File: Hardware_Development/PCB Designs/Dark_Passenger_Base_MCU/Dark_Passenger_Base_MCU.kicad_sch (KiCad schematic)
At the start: 26 parts, among them J1 Conn_01x22, J10 SPARE I2C, J11 IMU, J12 Toggle Switches, J13 Spare, J14 Motor Encoder 1, J15 Motor Encoder 2, J16 RESET, J18 Motor Control, J2 Conn_01x22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

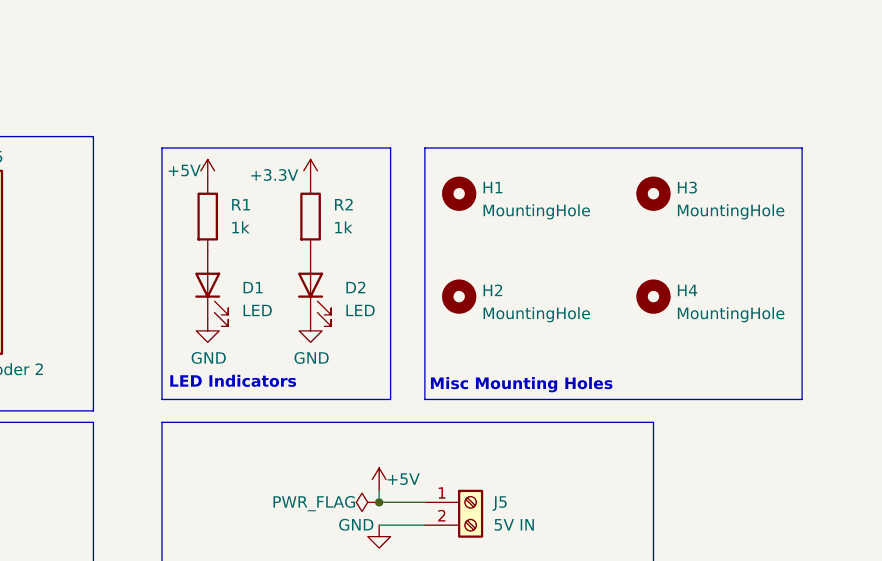
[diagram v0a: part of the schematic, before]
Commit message: Updates to code based on new pinouts from PCBs
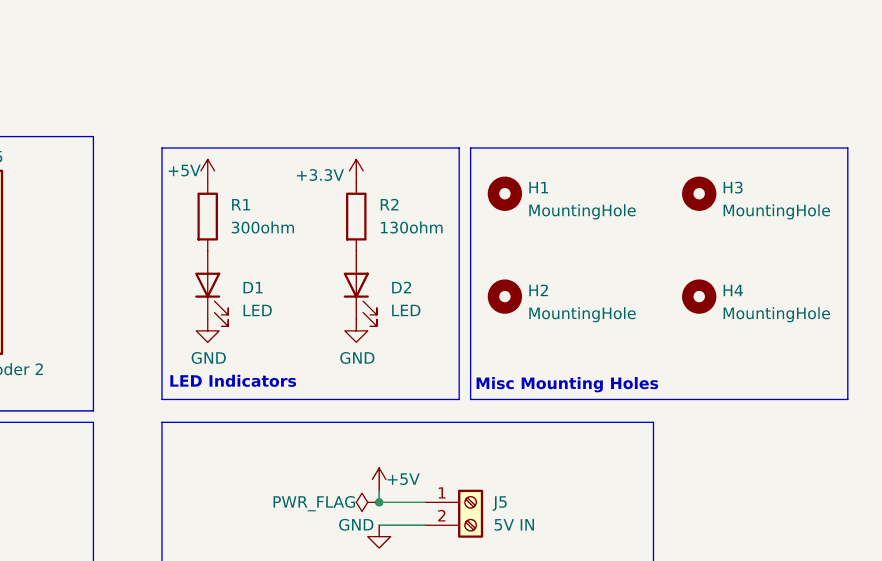
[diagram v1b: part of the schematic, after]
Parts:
- R1: value 1k -> 300ohm
- R2: value 1k -> 130ohm
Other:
- moved on the sheet: D2, H1, H2, H3, H4, R2
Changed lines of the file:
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@@
 	(rectangle
 		(start 175.26 26.67)
-		(end 200.66 54.61)
+		(end 208.28 54.61)
 		(stroke
 			(width 0)
@@
 	)
 	(rectangle
-		(start 204.47 26.67)
-		(end 246.38 54.61)
+		(start 209.55 26.67)
+		(end 251.46 54.61)
 		(stroke
 			(width 0)
@@
 	(text "Misc Mounting Holes"
 		(exclude_from_sim no)
-		(at 204.978 53.848 0)
+		(at 210.058 53.848 0)
 		(effects
 			(font
@@
 		(on_board yes)
 		(dnp no)
-		(fields_autoplaced yes)
 		(property "Reference" "R1"
 			(at 182.88 33.0199 0)
@@
 			)
 		)
-		(property "Value" "1k"
+		(property "Value" "300ohm"
 			(at 182.88 35.5599 0)
 			(effects
@@
 	(symbol
 		(lib_id "Device:R")
-		(at 191.77 34.29 0)
+		(at 196.85 34.29 0)
 		(unit 1)
 		(exclude_from_sim no)
@@
 		(fields_autoplaced yes)
 		(property "Reference" "R2"
-			(at 194.31 33.0199 0)
+			(at 199.39 33.0199 0)
 			(effects
 				(font
@@
 			)
 		)
-		(property "Value" "1k"
-			(at 194.31 35.5599 0)
+		(property "Value" "130ohm"
+			(at 199.39 35.5599 0)
 			(effects
 				(font
@@
 		)
 		(property "Footprint" "Resistor_SMD:R_1206_3216Metric_Pad1.30x1.75mm_HandSolder"
-			(at 189.992 34.29 90)
+			(at 195.072 34.29 90)
 			(effects
 				(font
@@
 		)
 		(property "Datasheet" "~"
-			(at 191.77 34.29 0)
+			(at 196.85 34.29 0)
 			(effects
 				(font
@@
 		)
 		(property "Description" ""
-			(at 191.77 34.29 0)
+			(at 196.85 34.29 0)
 			(effects
 				(font
@@
 	(symbol
 		(lib_id "power:GND")
-		(at 191.77 45.72 0)
+		(at 196.85 45.72 0)
 		(unit 1)
 		(exclude_from_sim no)
@@
 		(dnp no)
 		(property "Reference" "#PWR028"
-			(at 191.77 52.07 0)
+			(at 196.85 52.07 0)
 			(effects
 				(font
@@
 		)
 		(property "Value" "GND"
-			(at 191.8843 50.0444 0)
+			(at 196.9643 50.0444 0)
 			(effects
 				(font
@@
 		)
 		(property "Footprint" ""
-			(at 191.77 45.72 0)
+			(at 196.85 45.72 0)
 			(effects
 				(font
@@
 		)
 		(property "Datasheet" ""
-			(at 191.77 45.72 0)
+			(at 196.85 45.72 0)
 			(effects
 				(font
@@
 		)
 		(property "Description" ""
-			(at 191.77 45.72 0)
+			(at 196.85 45.72 0)
 			(effects
 				(font
@@
 	(symbol
 		(lib_id "Mechanical:MountingHole")
-		(at 208.28 43.18 0)
+		(at 213.36 43.18 0)
 		(unit 1)
 		(exclude_from_sim no)
@@
 		(dnp no)
 		(property "Reference" "H2"
-			(at 210.82 42.545 0)
+			(at 215.9 42.545 0)
 			(effects
 				(font
@@
 		)
 		(property "Value" "MountingHole"
-			(at 210.82 45.085 0)
+			(at 215.9 45.085 0)
 			(effects
 				(font
@@
 		)
 		(property "Footprint" "MountingHole:MountingHole_3mm"
-			(at 208.28 43.18 0)
+			(at 213.36 43.18 0)
 			(effects
 				(font
@@
 		)
 		(property "Datasheet" "~"
-			(at 208.28 43.18 0)
+			(at 213.36 43.18 0)
 			(effects
 				(font
@@
 		)
 		(property "Description" ""
-			(at 208.28 43.18 0)
+			(at 213.36 43.18 0)
 			(effects
 				(font
@@
 	(symbol
 		(lib_id "Mechanical:MountingHole")
-		(at 208.28 31.75 0)
+		(at 213.36 31.75 0)
 		(unit 1)
 		(exclude_from_sim no)
@@
 		(dnp no)
 		(property "Reference" "H1"
-			(at 210.82 31.115 0)
+			(at 215.9 31.115 0)
 			(effects
 				(font
@@
 		)
 		(property "Value" "MountingHole"
-			(at 210.82 33.655 0)
+			(at 215.9 33.655 0)
 			(effects
 				(font
@@
 		)
 		(property "Footprint" "MountingHole:MountingHole_3mm"
-			(at 208.28 31.75 0)
+			(at 213.36 31.75 0)
 			(effects
 				(font
@@
 		)
 		(property "Datasheet" "~"
-			(at 208.28 31.75 0)
+			(at 213.36 31.75 0)
 			(effects
 				(font
@@
 		)
 		(property "Description" ""
-			(at 208.28 31.75 0)
+			(at 213.36 31.75 0)
 			(effects
 				(font
@@
 		(lib_name "LED_1")
 		(lib_id "Device:LED")
-		(at 191.77 41.91 90)
+		(at 196.85 41.91 90)
 		(unit 1)
 		(exclude_from_sim no)
@@
 		(fields_autoplaced yes)
 		(property "Reference" "D2"
-			(at 195.58 42.2274 90)
+			(at 200.66 42.2274 90)
 			(effects
 				(font
@@
 		)
 		(property "Value" "LED"
-			(at 195.58 44.7674 90)
+			(at 200.66 44.7674 90)
 			(effects
 				(font
@@
 		)
 		(property "Footprint" "LED_SMD:LED_1206_3216Metric_Pad1.42x1.75mm_HandSolder"
-			(at 191.77 41.91 0)
+			(at 196.85 41.91 0)
 			(effects
 				(font
@@
 		)
 		(property "Datasheet" "~"
-			(at 191.77 41.91 0)
+			(at 196.85 41.91 0)
 			(effects
 				(font
@@
 		)
 		(property "Description" "Light emitting diode"
-			(at 191.77 41.91 0)
+			(at 196.85 41.91 0)
 			(effects
 				(font
@@
 		)
 		(property "Sim.Pins" "1=K 2=A"
-			(at 191.77 41.91 0)
+			(at 196.85 41.91 0)
 			(effects
 				(font
@@
 	(symbol
 		(lib_id "power:+3.3V")
-		(at 191.77 30.48 0)
+		(at 196.85 30.48 0)
 		(unit 1)
 		(exclude_from_sim no)
@@
 		(dnp no)
 		(property "Reference" "#PWR041"
-			(at 191.77 34.29 0)
+			(at 196.85 34.29 0)
 			(effects
 				(font
@@
 		)
 		(property "Value" "+3.3V"
-			(at 187.706 29.718 0)
+			(at 192.786 29.718 0)
 			(effects
 				(font
@@
 		)
 		(property "Footprint" ""
-			(at 191.77 30.48 0)
+			(at 196.85 30.48 0)
 			(effects
 				(font
@@
 		)
 		(property "Datasheet" ""
-			(at 191.77 30.48 0)
+			(at 196.85 30.48 0)
 			(effects
 				(font
@@
 		)
 		(property "Description" "Power symbol creates a global label with name \"+3.3V\""
-			(at 191.77 30.48 0)
+			(at 196.85 30.48 0)
 			(effects
 				(font
@@
 	(symbol
 		(lib_id "Mechanical:MountingHole")
-		(at 229.87 43.18 0)
+		(at 234.95 43.18 0)
 		(unit 1)
 		(exclude_from_sim no)
@@
 		(dnp no)
 		(property "Reference" "H4"
-			(at 232.41 42.545 0)
+			(at 237.49 42.545 0)
 			(effects
 				(font
@@
 		)
 		(property "Value" "MountingHole"
-			(at 232.41 45.085 0)
+			(at 237.49 45.085 0)
 			(effects
 				(font
@@
 		)
 		(property "Footprint" "MountingHole:MountingHole_3mm"
-			(at 229.87 43.18 0)
+			(at 234.95 43.18 0)
 			(effects
 				(font
@@
 		)
 		(property "Datasheet" "~"
-			(at 229.87 43.18 0)
+			(at 234.95 43.18 0)
 			(effects
 				(font
@@
 		)
 		(property "Description" ""
-			(at 229.87 43.18 0)
+			(at 234.95 43.18 0)
 			(effects
 				(font
@@
 	(symbol
 		(lib_id "Mechanical:MountingHole")
-		(at 229.87 31.75 0)
+		(at 234.95 31.75 0)
 		(unit 1)
 		(exclude_from_sim no)
@@
 		(fields_autoplaced yes)
 		(property "Reference" "H3"
-			(at 232.41 31.115 0)
+			(at 237.49 31.115 0)
 			(effects
 				(font
@@
 		)
 		(property "Value" "MountingHole"
-			(at 232.41 33.655 0)
+			(at 237.49 33.655 0)
 			(effects
 				(font
@@
 		)
 		(property "Footprint" "MountingHole:MountingHole_3mm"
-			(at 229.87 31.75 0)
+			(at 234.95 31.75 0)
 			(effects
 				(font
@@
 		)
 		(property "Datasheet" "~"
-			(at 229.87 31.75 0)
+			(at 234.95 31.75 0)
 			(effects
 				(font
@@
 		)
 		(property "Description" ""
-			(at 229.87 31.75 0)
+			(at 234.95 31.75 0)
 			(effects
 				(font
